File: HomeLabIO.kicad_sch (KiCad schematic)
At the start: 0 parts

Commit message: chore: schematic PDF and iBOM
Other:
- title: (none) -> HomeLabIO
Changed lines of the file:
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@@
 	(generator_version "9.0")
 	(paper "A4")
+	(title_block
+		(title "HomeLabIO")
+		(rev "v0.3")
+	)
 	(bus
 		(pts

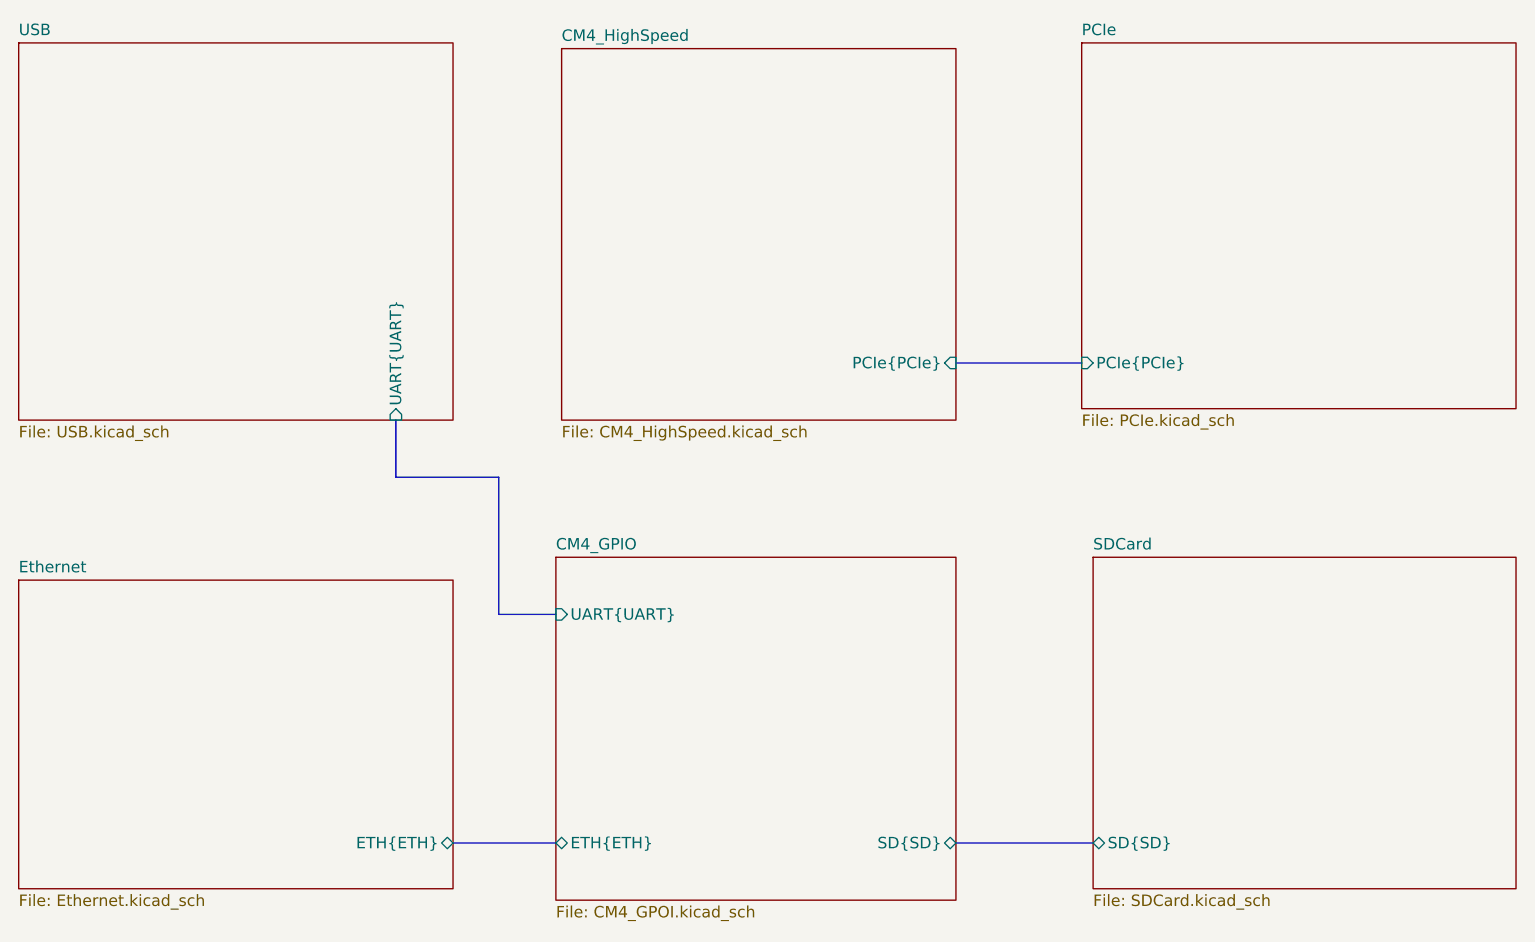
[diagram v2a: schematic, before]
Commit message: feat: use hardware components
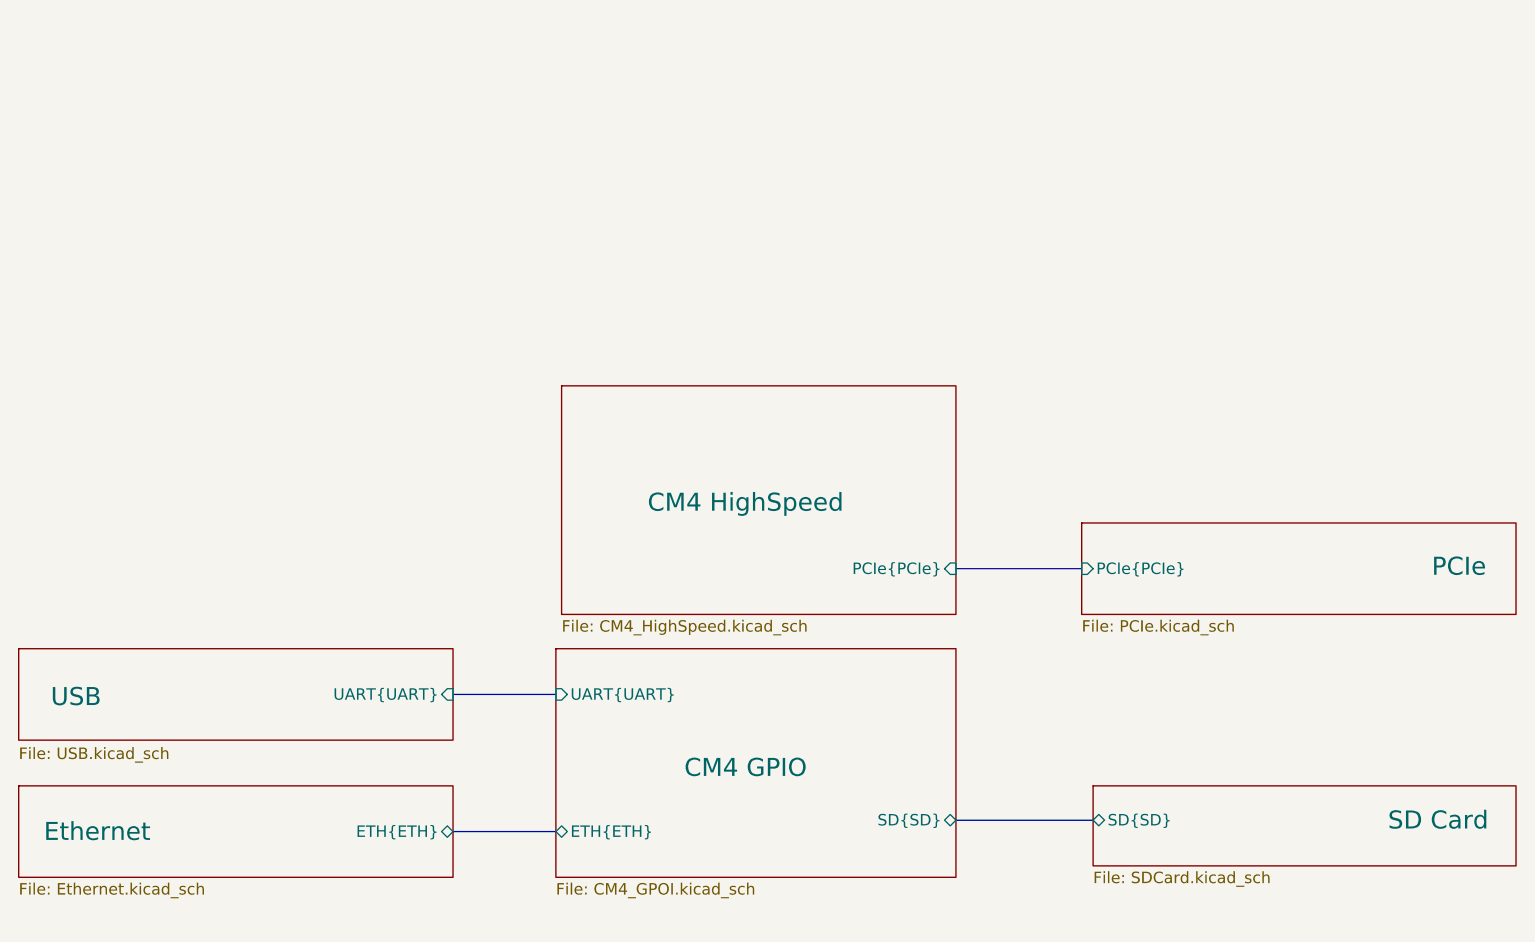
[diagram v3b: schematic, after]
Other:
- sheet CM4_GPIO renamed CM4 GPIO
- sheet CM4_HighSpeed renamed CM4 HighSpeed
- sheet SDCard renamed SD Card
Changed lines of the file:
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@@
 	(bus
 		(pts
-			(xy 166.37 67.31) (xy 180.34 67.31)
+			(xy 110.49 104.14) (xy 121.92 104.14)
 		)
 		(stroke
@@
 	(bus
 		(pts
-			(xy 115.57 95.25) (xy 115.57 80.01)
+			(xy 166.37 90.17) (xy 180.34 90.17)
 		)
 		(stroke
@@
 	(bus
 		(pts
-			(xy 121.92 95.25) (xy 115.57 95.25)
+			(xy 110.49 119.38) (xy 121.92 119.38)
 		)
 		(stroke
@@
 	(bus
 		(pts
-			(xy 110.49 120.65) (xy 121.92 120.65)
+			(xy 166.37 118.11) (xy 181.61 118.11)
 		)
 		(stroke
@@
 		)
 	)
-	(bus
-		(pts
-			(xy 166.37 120.65) (xy 181.61 120.65)
-		)
-		(stroke
-			(width 0)
-			(type default)
-		)
-	)
-	(bus
-		(pts
-			(xy 104.14 80.01) (xy 104.14 73.66)
-		)
-		(stroke
-			(width 0)
-			(type default)
-		)
-	)
-	(bus
-		(pts
-			(xy 115.57 80.01) (xy 104.14 80.01)
-		)
-		(stroke
-			(width 0)
-			(type default)
-		)
-	)
-	(sheet
-		(at 122.555 32.385)
-		(size 43.815 41.275)
-		(exclude_from_sim no)
-		(in_bom yes)
-		(on_board yes)
-		(dnp no)
-		(fields_autoplaced yes)
-		(stroke
-			(width 0.1524)
-			(type solid)
-		)
-		(fill
-			(color 0 0 0 0.0000)
-		)
-		(property "Sheetname" "CM4_HighSpeed"
-			(at 122.555 31.6734 0)
-			(effects
-				(font
-					(size 1.27 1.27)
-				)
-				(justify left bottom)
+	(sheet
+		(at 122.555 69.85)
+		(size 43.815 25.4)
+		(exclude_from_sim no)
+		(in_bom yes)
+		(on_board yes)
+		(dnp no)
+		(stroke
+			(width 0.1524)
+			(type solid)
+		)
+		(fill
+			(color 0 0 0 0.0000)
+		)
+		(property "Sheetname" "CM4 HighSpeed"
+			(at 143.002 82.804 0)
+			(effects
+				(font
+					(size 2 2)
+				)
 			)
 		)
 		(property "Sheetfile" "CM4_HighSpeed.kicad_sch"
-			(at 122.555 74.2446 0)
+			(at 122.555 95.8346 0)
 			(effects
 				(font
@@
 		)
 		(pin "PCIe{PCIe}" input
-			(at 166.37 67.31 0)
+			(at 166.37 90.17 0)
 			(effects
 				(font
@@
 	)
 	(sheet
-		(at 62.23 31.75)
-		(size 48.26 41.91)
-		(exclude_from_sim no)
-		(in_bom yes)
-		(on_board yes)
-		(dnp no)
-		(fields_autoplaced yes)
+		(at 62.23 99.06)
+		(size 48.26 10.16)
+		(exclude_from_sim no)
+		(in_bom yes)
+		(on_board yes)
+		(dnp no)
 		(stroke
 			(width 0.1524)
@@
 		)
 		(property "Sheetname" "USB"
-			(at 62.23 31.0384 0)
-			(effects
-				(font
-					(size 1.27 1.27)
-				)
-				(justify left bottom)
+			(at 65.786 104.394 0)
+			(effects
+				(font
+					(size 2 2)
+				)
+				(justify left)
 			)
 		)
 		(property "Sheetfile" "USB.kicad_sch"
-			(at 62.23 74.2446 0)
+			(at 62.23 109.982 0)
 			(effects
 				(font
@@
 		)
 		(pin "UART{UART}" input
-			(at 104.14 73.66 270)
-			(effects
-				(font
-					(size 1.27 1.27)
-				)
-				(justify left)
+			(at 110.49 104.14 0)
+			(effects
+				(font
+					(size 1.27 1.27)
+				)
+				(justify right)
 			)
 		)
@@
 	)
 	(sheet
-		(at 62.23 91.44)
-		(size 48.26 34.29)
-		(exclude_from_sim no)
-		(in_bom yes)
-		(on_board yes)
-		(dnp no)
-		(fields_autoplaced yes)
+		(at 62.23 114.3)
+		(size 48.26 10.16)
+		(exclude_from_sim no)
+		(in_bom yes)
+		(on_board yes)
+		(dnp no)
 		(stroke
 			(width 0.1524)
@@
 		)
 		(property "Sheetname" "Ethernet"
-			(at 62.23 90.7284 0)
-			(effects
-				(font
-					(size 1.27 1.27)
-				)
-				(justify left bottom)
+			(at 65.024 119.38 0)
+			(effects
+				(font
+					(size 2 2)
+				)
+				(justify left)
 			)
 		)
 		(property "Sheetfile" "Ethernet.kicad_sch"
-			(at 62.23 126.3146 0)
+			(at 62.23 125.0446 0)
 			(effects
 				(font
@@
 		)
 		(pin "ETH{ETH}" bidirectional
-			(at 110.49 120.65 0)
+			(at 110.49 119.38 0)
 			(effects
 				(font
@@
 	)
 	(sheet
-		(at 181.61 88.9)
-		(size 46.99 36.83)
-		(exclude_from_sim no)
-		(in_bom yes)
-		(on_board yes)
-		(dnp no)
-		(fields_autoplaced yes)
-		(stroke
-			(width 0.1524)
-			(type solid)
-		)
-		(fill
-			(color 0 0 0 0.0000)
-		)
-		(property "Sheetname" "SDCard"
-			(at 181.61 88.1884 0)
-			(effects
-				(font
-					(size 1.27 1.27)
-				)
-				(justify left bottom)
+		(at 181.61 114.3)
+		(size 46.99 8.89)
+		(exclude_from_sim no)
+		(in_bom yes)
+		(on_board yes)
+		(dnp no)
+		(stroke
+			(width 0.1524)
+			(type solid)
+		)
+		(fill
+			(color 0 0 0 0.0000)
+		)
+		(property "Sheetname" "SD Card"
+			(at 225.552 118.11 0)
+			(effects
+				(font
+					(size 2 2)
+				)
+				(justify right)
 			)
 		)
 		(property "Sheetfile" "SDCard.kicad_sch"
-			(at 181.61 126.3146 0)
+			(at 181.61 123.7746 0)
 			(effects
 				(font
@@
 		)
 		(pin "SD{SD}" bidirectional
-			(at 181.61 120.65 180)
+			(at 181.61 118.11 180)
 			(effects
 				(font
@@
 	)
 	(sheet
-		(at 121.92 88.9)
-		(size 44.45 38.1)
-		(exclude_from_sim no)
-		(in_bom yes)
-		(on_board yes)
-		(dnp no)
-		(fields_autoplaced yes)
-		(stroke
-			(width 0.1524)
-			(type solid)
-		)
-		(fill
-			(color 0 0 0 0.0000)
-		)
-		(property "Sheetname" "CM4_GPIO"
-			(at 121.92 88.1884 0)
-			(effects
-				(font
-					(size 1.27 1.27)
-				)
-				(justify left bottom)
+		(at 121.92 99.06)
+		(size 44.45 25.4)
+		(exclude_from_sim no)
+		(in_bom yes)
+		(on_board yes)
+		(dnp no)
+		(stroke
+			(width 0.1524)
+			(type solid)
+		)
+		(fill
+			(color 0 0 0 0.0000)
+		)
+		(property "Sheetname" "CM4 GPIO"
+			(at 143.002 112.268 0)
+			(effects
+				(font
+					(size 2 2)
+				)
 			)
 		)
 		(property "Sheetfile" "CM4_GPOI.kicad_sch"
-			(at 121.92 127.5846 0)
+			(at 121.92 125.0446 0)
 			(effects
 				(font
@@
 		)
 		(pin "ETH{ETH}" bidirectional
-			(at 121.92 120.65 180)
+			(at 121.92 119.38 180)
 			(effects
 				(font
@@
 		)
 		(pin "SD{SD}" bidirectional
-			(at 166.37 120.65 0)
+			(at 166.37 118.11 0)
 			(effects
 				(font
@@
 		)
 		(pin "UART{UART}" input
-			(at 121.92 95.25 180)
+			(at 121.92 104.14 180)
 			(effects
 				(font
@@
 	)
 	(sheet
-		(at 180.34 31.75)
-		(size 48.26 40.64)
-		(exclude_from_sim no)
-		(in_bom yes)
-		(on_board yes)
-		(dnp no)
-		(fields_autoplaced yes)
+		(at 180.34 85.09)
+		(size 48.26 10.16)
+		(exclude_from_sim no)
+		(in_bom yes)
+		(on_board yes)
+		(dnp no)
 		(stroke
 			(width 0.1524)
@@
 		)
 		(property "Sheetname" "PCIe"
-			(at 180.34 31.0384 0)
-			(effects
-				(font
-					(size 1.27 1.27)
-				)
-				(justify left bottom)
+			(at 225.298 89.916 0)
+			(effects
+				(font
+					(size 2 2)
+				)
+				(justify right)
 			)
 		)
 		(property "Sheetfile" "PCIe.kicad_sch"
-			(at 180.34 72.9746 0)
+			(at 180.34 95.8346 0)
 			(effects
 				(font
@@
 		)
 		(pin "PCIe{PCIe}" input
-			(at 180.34 67.31 180)
-			(effects
-				(font
+			(at 180.34 90.17 180)
+			(effects
+				(font
